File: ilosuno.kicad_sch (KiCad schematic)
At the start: 46 parts, among them J1 2.54MM_PADS, J2 KF350, J3 2.54MM_PADS, J4 KF350, Q1 IRLR7843TRPBF, Q2 AO3400A, Q3 AO3400A, Q4 IRLR7843TRPBF, Q5 AO3400A, Q6 IRLR7843TRPBF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

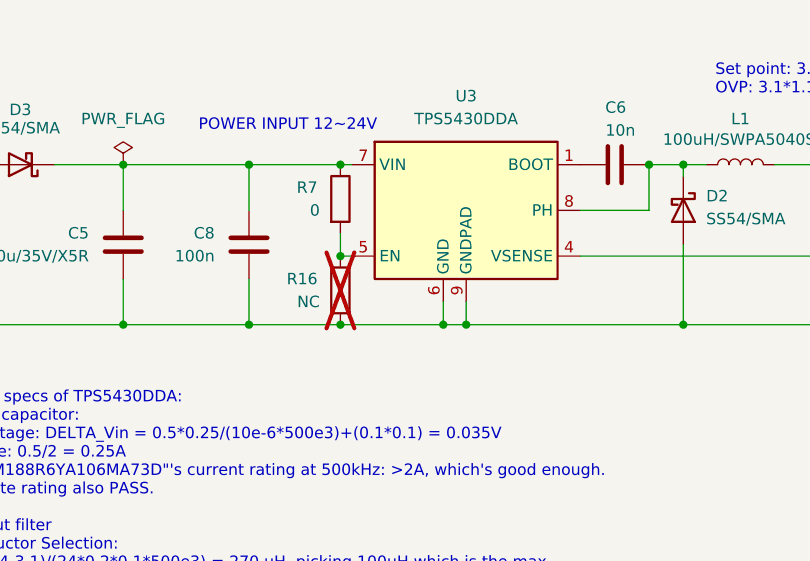
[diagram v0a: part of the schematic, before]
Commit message: Bug fixed: Buck converter EN pin overvoltage
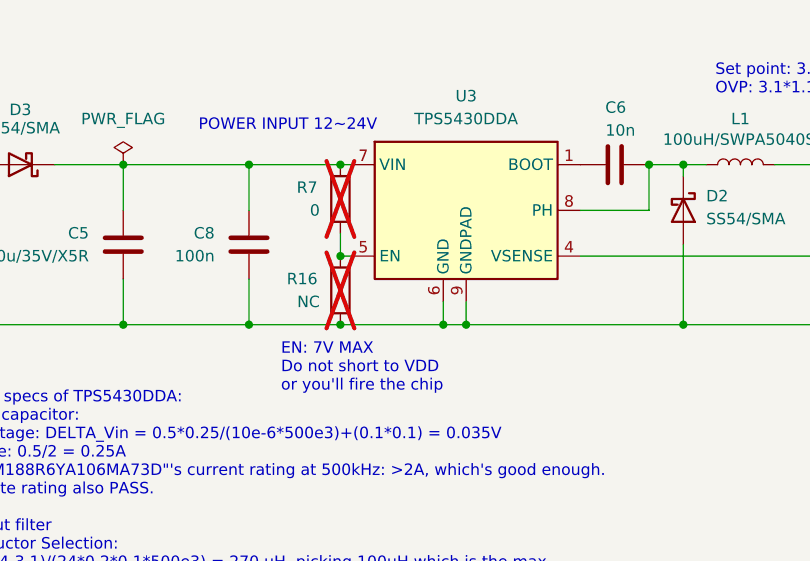
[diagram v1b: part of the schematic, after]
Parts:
- R7: now not fitted
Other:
- note added: "EN: 7V MAX Do not short to VDD or you'll fire the chip"
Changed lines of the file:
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@@
 		)
 	)
+	(text "EN: 7V MAX\nDo not short to VDD\nor you'll fire the chip"
+		(exclude_from_sim no)
+		(at 65.786 59.436 0)
+		(effects
+			(font
+				(size 1.27 1.27)
+			)
+			(justify left)
+		)
+	)
 	(text "NodeMCU D0"
 		(exclude_from_sim no)
@@
 		(in_bom yes)
 		(on_board yes)
-		(dnp no)
+		(dnp yes)
 		(property "Reference" "R7"
 			(at 69.85 39.3699 0)
